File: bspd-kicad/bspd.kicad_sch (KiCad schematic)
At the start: 118 parts, among them J1 Conn_02x04_Counter_Clockwise, Q1 AO3400A, Q2 AO3401A, SW1 CJS-1200TB1, SW2 CJS-1200TB1, U5 SN74HC74DR, U6 LM1117MP-5.0, U7 SN74LVC2G14DBVR, U8 SN74LVC3G14DCUR, U9 SN74LVC3G14DCUR

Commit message: all issues addressed
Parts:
- U7: footprint Package_SO:VSSOP-8_3x3mm_P0.65mm -> bspd:SN74LVC2G14DBVR
- U8, U9: footprint Package_SO:VSSOP-8_3x3mm_P0.65mm -> bspd:SN74LVC3G14DCUR
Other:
- moved on the sheet: D11, D13, D14, R41, R43, R44, U9A, U9B, U9C

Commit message: Fixed library issue
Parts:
- D2, D3, D4: symbol apppd:AQ1005-01ETG -> bspd:AQ1005-01ETG
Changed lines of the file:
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@@
 	)
 	(symbol
-		(lib_id "apppd:AQ1005-01ETG")
+		(lib_id "bspd:AQ1005-01ETG")
 		(at 38.1 54.61 270)
 		(unit 1)
@@
 	)
 	(symbol
-		(lib_id "apppd:AQ1005-01ETG")
+		(lib_id "bspd:AQ1005-01ETG")
 		(at 38.1 68.58 270)
 		(unit 1)
@@
 	)
 	(symbol
-		(lib_id "apppd:AQ1005-01ETG")
+		(lib_id "bspd:AQ1005-01ETG")
 		(at 38.1 40.64 270)
 		(unit 1)

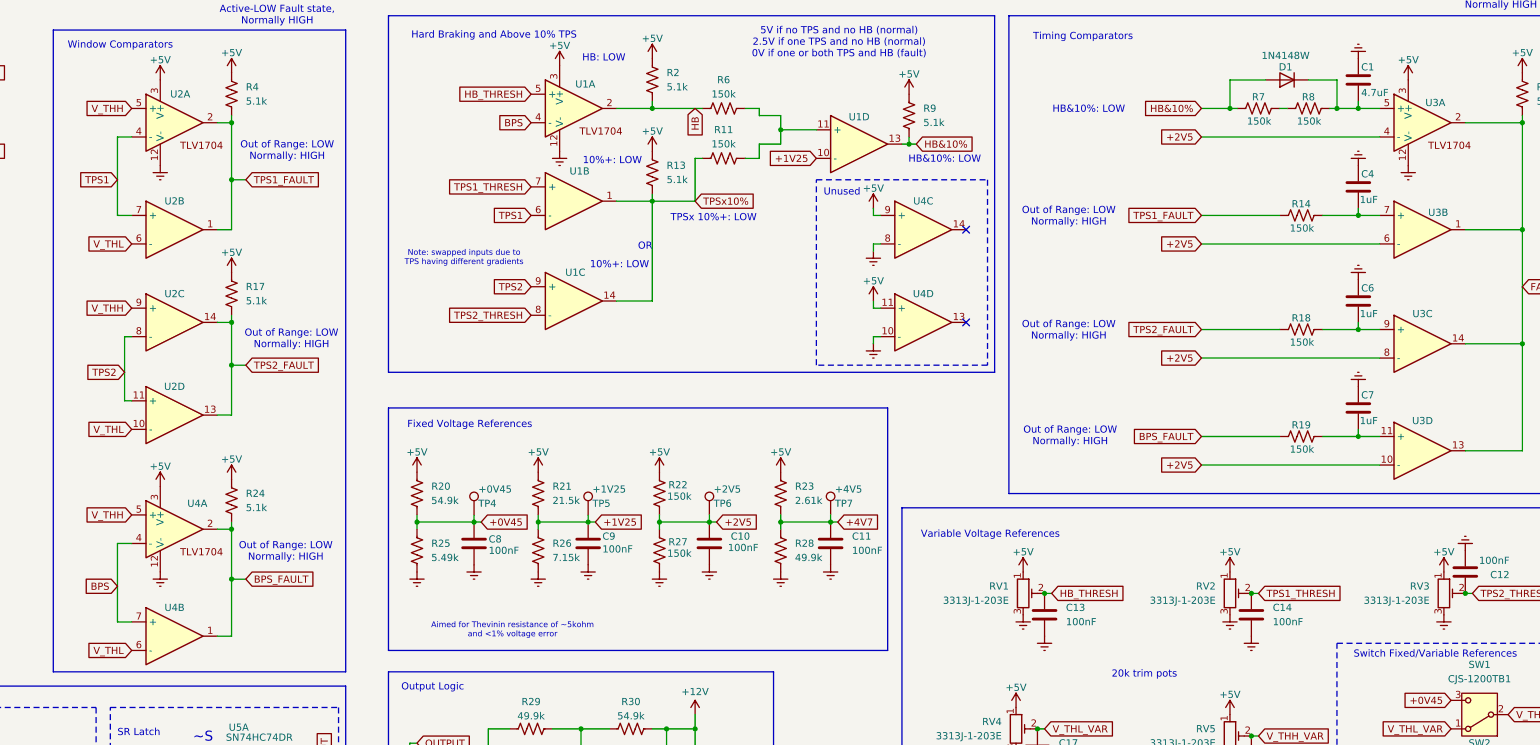
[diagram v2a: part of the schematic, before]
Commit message: Move GND earth symbol into project library; complete BOM fields
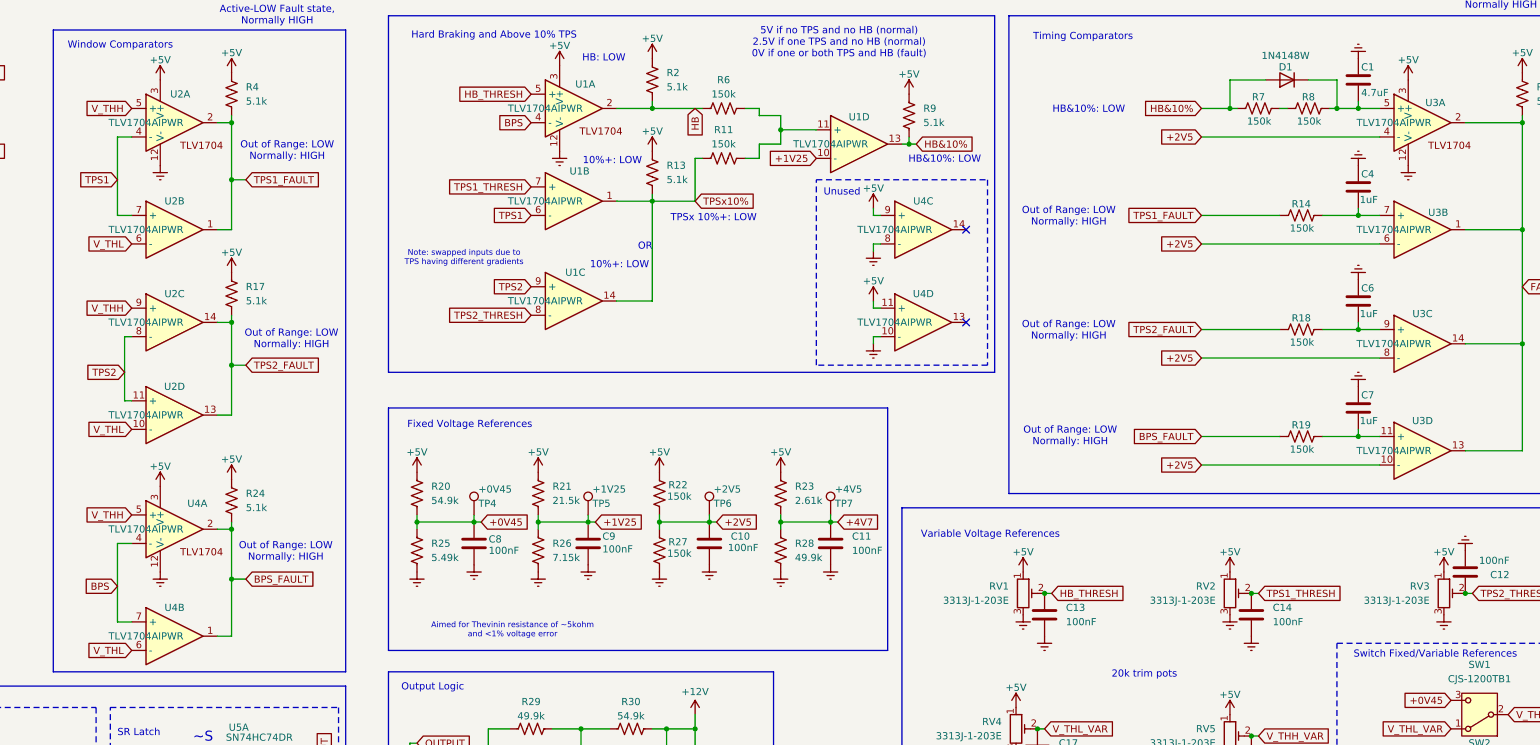
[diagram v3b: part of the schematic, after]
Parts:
- C1, C10, C11, C12, C13, C14, C16, C17, C18, C19, C2, C20, C21, C22, C23, C24, C25, C26, C27, C28, C3, C4, C5, C6, C7, C8, C9: Dielectric (none) -> X7R; Tolerance (none) -> 10%; Voltage (none) -> 16V
- C15: Dielectric (none) -> X7R; Tolerance (none) -> 10%; Voltage (none) -> 25V
- R1, R10, R11, R12, R13, R14, R15, R16, R17, R18, R19, R2, R20, R21, R22, R23, R24, R25, R26, R27, R28, R29, R3, R30, R31, R32, R33, R34, R35, R36, R37, R38, R39, R4, R40, R41, R42, R43, R44, R45, R5, R6, R7, R8, R9: Tolerance (none) -> 1%
- RV1, RV2, RV3, RV4, RV5: symbol bspd:3313J-1-103E -> bspd:3313J-1-203E; LCSC Part C124616 -> C124621; MPN 3313J-1-103E -> 3313J-1-203E; Resistance 10k -> 20k; Tolerance (none) -> 20%
- U1, U2, U3, U4: value (none) -> TLV1704AIPWR; MPN (none) -> TLV1704AIPWR; Manufacturer (none) -> Texas Instruments

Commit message: ERC issues addressed
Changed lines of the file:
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@@
 	)
 	(symbol
-		(lib_name "TLV1704_1")
 		(lib_id "bspd:TLV1704")
 		(at 355.6 85.09 0)
@@
 	)
 	(symbol
-		(lib_name "TLV1704_1")
 		(lib_id "bspd:TLV1704")
 		(at 355.6 104.14 0)
@@
 	)
 	(symbol
-		(lib_name "TLV1704_1")
 		(lib_id "bspd:TLV1704")
 		(at 355.6 45.72 0)
@@
 	)
 	(symbol
-		(lib_name "TLV1704_1")
 		(lib_id "bspd:TLV1704")
 		(at 355.6 64.77 0)
@@
 		)
 	)
+	(symbol
+		(lib_id "power:PWR_FLAG")
+		(at 46.99 85.09 0)
+		(unit 1)
+		(body_style 1)
+		(exclude_from_sim no)
+		(in_bom yes)
+		(on_board yes)
+		(in_pos_files yes)
+		(dnp no)
+		(fields_autoplaced yes)
+		(property "Reference" "#FLG01"
+			(at 46.99 83.185 0)
+			(hide yes)
+			(show_name no)
+			(do_not_autoplace no)
+			(effects
+				(font
+					(size 1.27 1.27)
+				)
+			)
+		)
+		(property "Value" "PWR_FLAG"
+			(at 46.99 81.28 0)
+			(hide yes)
+			(show_name no)
+			(do_not_autoplace no)
+			(effects
+				(font
+					(size 1.27 1.27)
+				)
+			)
+		)
+		(property "Footprint" ""
+			(at 46.99 85.09 0)
+			(hide yes)
+			(show_name no)
+			(do_not_autoplace no)
+			(effects
+				(font
+					(size 1.27 1.27)
+				)
+			)
+		)
+		(property "Datasheet" ""
+			(at 46.99 85.09 0)
+			(hide yes)
+			(show_name no)
+			(do_not_autoplace no)
+			(effects
+				(font
+					(size 1.27 1.27)
+				)
+			)
+		)
+		(property "Description" "Special symbol for telling ERC where power comes from"
+			(at 46.99 85.09 0)
+			(hide yes)
+			(show_name no)
+			(do_not_autoplace no)
+			(effects
+				(font
+					(size 1.27 1.27)
+				)
+			)
+		)
+		(pin "1"
+		)
+		(instances
+			(project "bspd"
+				(path "/e8b8835b-5dd0-46e2-9a0c-fed9bbaa86de"
+					(reference "#FLG01")
+					(unit 1)
+				)
+			)
+		)
+	)
+	(wire
+		(pts
+			(xy 46.99 85.09) (xy 46.99 90.17)
+		)
+		(stroke
+			(width 0)
+			(type default)
+		)
+	)
+	(symbol
+		(lib_id "power:PWR_FLAG")
+		(at 349.25 29.21 0)
+		(unit 1)
+		(body_style 1)
+		(exclude_from_sim no)
+		(in_bom yes)
+		(on_board yes)
+		(in_pos_files yes)
+		(dnp no)
+		(fields_autoplaced yes)
+		(property "Reference" "#FLG02"
+			(at 349.25 27.305 0)
+			(hide yes)
+			(show_name no)
+			(do_not_autoplace no)
+			(effects
+				(font
+					(size 1.27 1.27)
+				)
+			)
+		)
+		(property "Value" "PWR_FLAG"
+			(at 349.25 25.4 0)
+			(hide yes)
+			(show_name no)
+			(do_not_autoplace no)
+			(effects
+				(font
+					(size 1.27 1.27)
+				)
+			)
+		)
+		(property "Footprint" ""
+			(at 349.25 29.21 0)
+			(hide yes)
+			(show_name no)
+			(do_not_autoplace no)
+			(effects
+				(font
+					(size 1.27 1.27)
+				)
+			)
+		)
+		(property "Datasheet" ""
+			(at 349.25 29.21 0)
+			(hide yes)
+			(show_name no)
+			(do_not_autoplace no)
+			(effects
+				(font
+					(size 1.27 1.27)
+				)
+			)
+		)
+		(property "Description" "Special symbol for telling ERC where power comes from"
+			(at 349.25 29.21 0)
+			(hide yes)
+			(show_name no)
+			(do_not_autoplace no)
+			(effects
+				(font
+					(size 1.27 1.27)
+				)
+			)
+		)
+		(pin "1"
+		)
+		(instances
+			(project "bspd"
+				(path "/e8b8835b-5dd0-46e2-9a0c-fed9bbaa86de"
+					(reference "#FLG02")
+					(unit 1)
+				)
+			)
+		)
+	)
+	(wire
+		(pts
+			(xy 349.25 29.21) (xy 349.25 34.29)
+		)
+		(stroke
+			(width 0)
+			(type default)
+		)
+	)

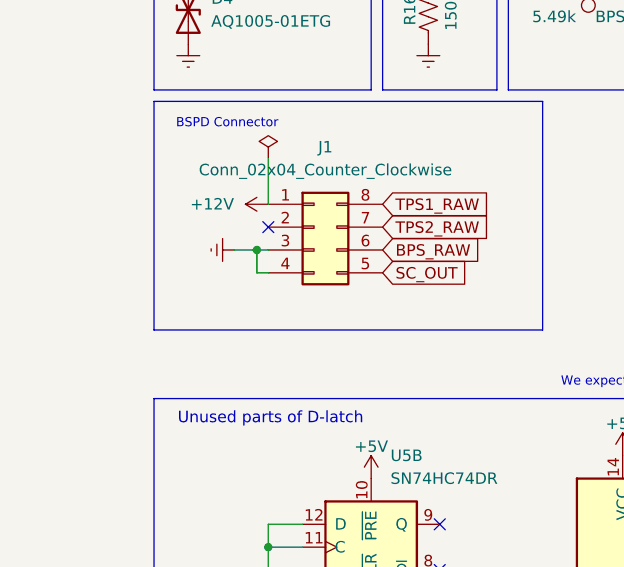
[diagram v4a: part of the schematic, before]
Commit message: Signal ground and chassis ground connected with 0 ohm resistor
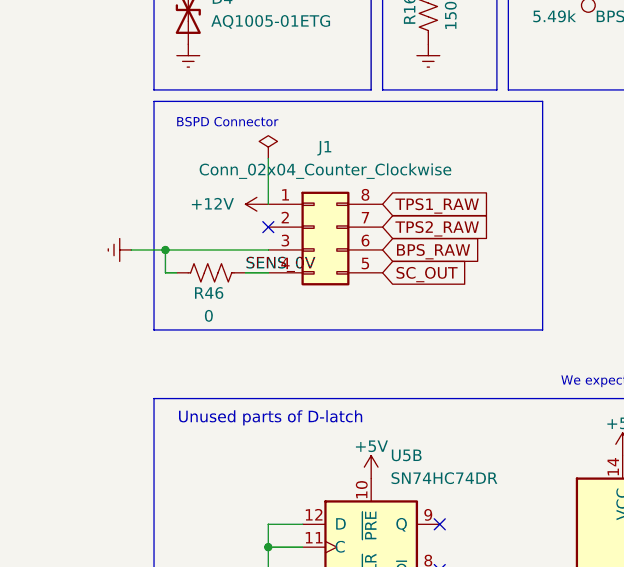
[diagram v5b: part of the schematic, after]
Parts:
- added R46: 0, Resistor_SMD:R_0805_2012Metric_Pad1.20x1.40mm_HandSolder, symbol Device:R_US
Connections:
- net GND: now also R46.1; no longer J1.4 (Pin_4)
- new net SENS_0V: J1.4 (Pin_4), R46.2

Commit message: Fix mislabeled RV1-RV5 trimmer footprint and remove unused duplicate diode footprint
The trimpot footprint was named/described as a 10k part when it's actually the 20k version used on the board; renamed it to match. Also removed a custom TVS diode footprint that was never used since D2-D4 already used KiCad's built-in equivalent footprint.
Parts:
- RV1, RV2, RV3, RV4, RV5: footprint bspd:3313J-1-103E -> bspd:3313J-1-203E
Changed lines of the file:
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@@
 			)
 		)
-		(property "Footprint" "bspd:3313J-1-103E"
+		(property "Footprint" "bspd:3313J-1-203E"
 			(at 326.39 154.94 0)
 			(hide yes)
@@
 			)
 		)
-		(property "Footprint" "bspd:3313J-1-103E"
+		(property "Footprint" "bspd:3313J-1-203E"
 			(at 326.39 129.54 0)
 			(hide yes)
@@
 			)
 		)
-		(property "Footprint" "bspd:3313J-1-103E"
+		(property "Footprint" "bspd:3313J-1-203E"
 			(at 289.56 129.54 0)
 			(hide yes)
@@
 			)
 		)
-		(property "Footprint" "bspd:3313J-1-103E"
+		(property "Footprint" "bspd:3313J-1-203E"
 			(at 364.49 129.54 0)
 			(hide yes)
@@
 			)
 		)
-		(property "Footprint" "bspd:3313J-1-103E"
+		(property "Footprint" "bspd:3313J-1-203E"
 			(at 288.29 153.67 0)
 			(hide yes)
